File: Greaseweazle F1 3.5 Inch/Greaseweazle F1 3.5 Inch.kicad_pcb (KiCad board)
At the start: 2 copper layers, 170.2 x 100 mm, 78 parts, among them CN1 Floppy Data, J1 USB B, J10 Conn_01x03, J11 Conn_01x03, J2 USB Header, J3 Floppy Power, J4 Floppy Power Header, J5 Programming Port, J6 SWD Port, J7 SWD Port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

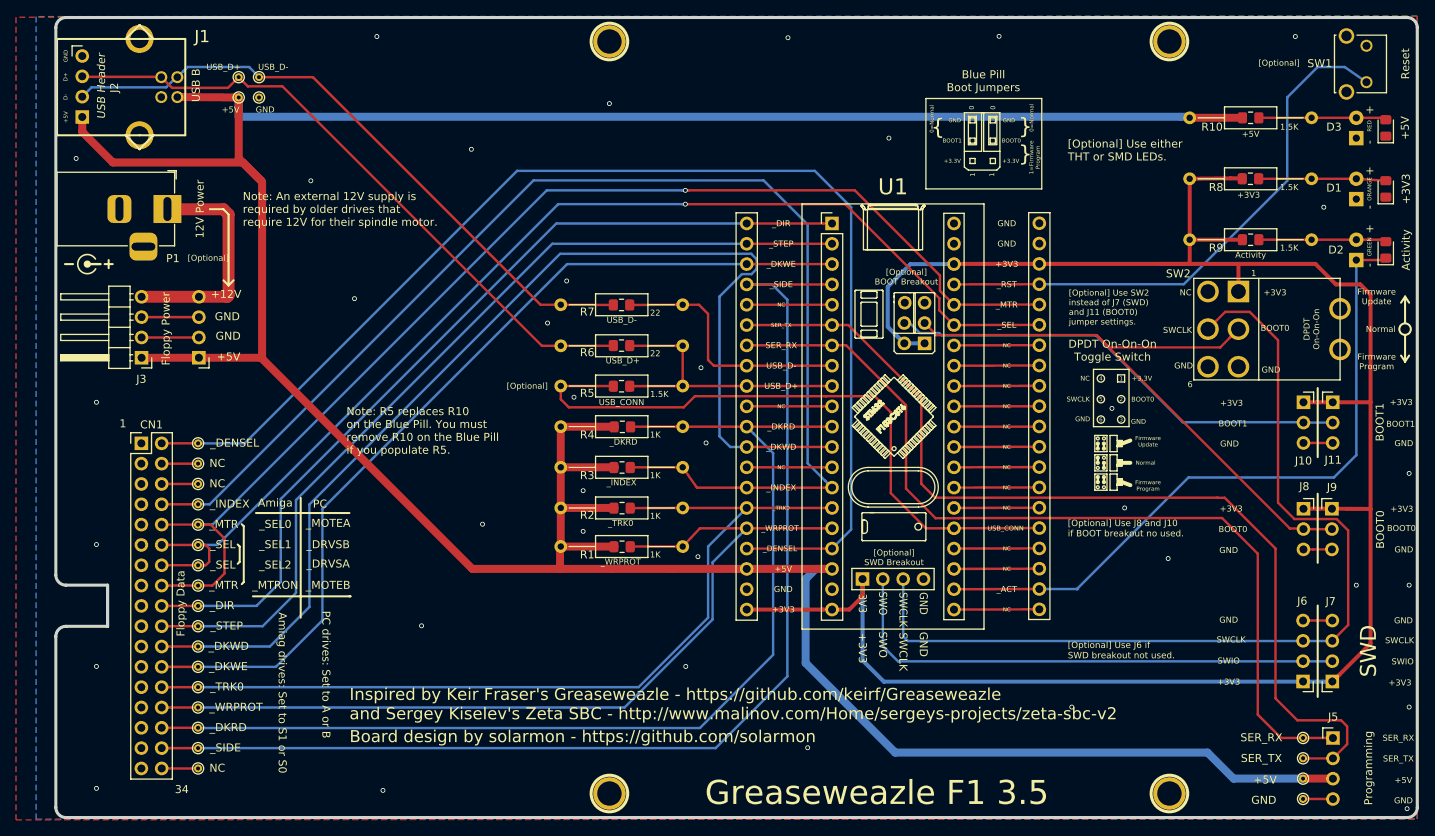
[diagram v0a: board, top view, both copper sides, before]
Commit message: Added 12V LED
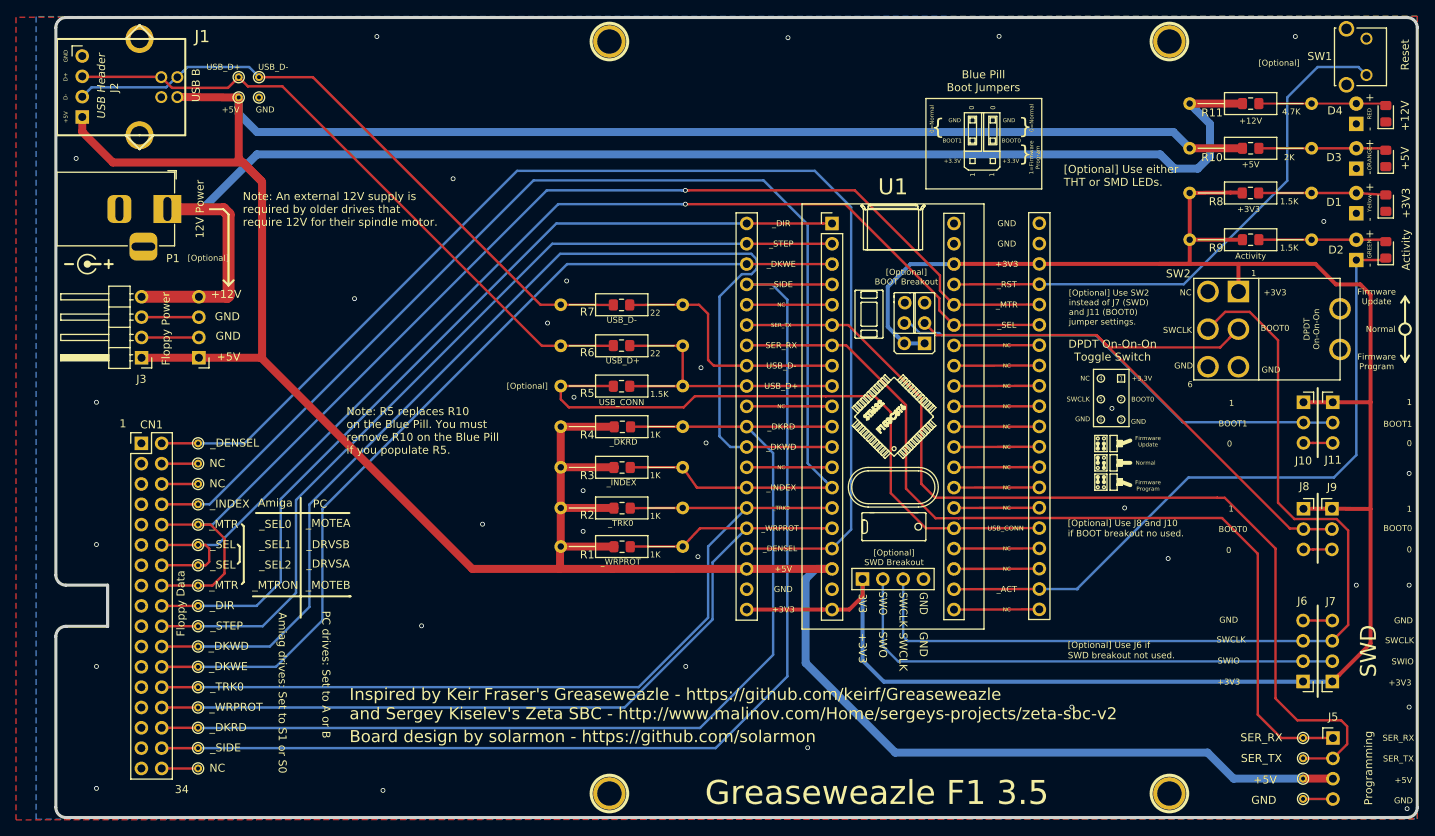
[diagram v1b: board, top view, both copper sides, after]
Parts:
- added D4: LED_D3.0mm_Horizontal_O1.27mm_Z6.0mm, LED_THT:LED_D3.0mm_Horizontal_O1.27mm_Z6.0mm, F.Cu at (213.4, 64.3)
- added D4: +5V LED, LED_SMD:LED_0805_2012Metric_Pad1.15x1.40mm_HandSolder, F.Cu at (217.0, 63.0)
- added R11: R_Axial_DIN0207_L6.3mm_D2.5mm_P15.24mm_Horizontal, Resistor_THT:R_Axial_DIN0207_L6.3mm_D2.5mm_P15.24mm_Horizontal, F.Cu at (207.8, 61.7)
- added R11: 4.7K, Resistor_SMD:R_0805_2012Metric_Pad1.15x1.40mm_HandSolder, F.Cu at (200.2, 61.7)
- R10: value 1.5K -> 2K
- SW2: value RS PRO DPDT Toggle Switch, On-On-On, PCB -> DPDT Toggle Switch, On-On-On, PCB
- moved D3 3.81 mm to (217.0, 68.6)
- moved R10 3.81 mm to (200.2, 67.3)
- moved R10 3.81 mm to (207.8, 67.3)
- moved D3 3.81 mm to (213.4, 69.8)
- moved D1 1.78 mm to (217.0, 74.2)
- moved D1 1.78 mm to (213.4, 75.4)
- moved R8 1.78 mm to (200.1, 72.9)
- moved R8 1.78 mm to (207.8, 72.9)
- moved SW1 0.89 mm to (214.6, 55.9)
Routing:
- net +12V: track 29.2 -> 178.0 mm
- net Net-(D4-Pad2): track 0.00 -> 16.0 mm
- net +5V: track 424.3 -> 425.7 mm
- net +3V3: track 259.2 -> 257.9 mm
- net GND: vias 37 -> 34
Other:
- board text added: "Yellow"
